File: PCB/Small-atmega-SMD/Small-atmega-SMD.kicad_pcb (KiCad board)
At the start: 2 copper layers, 65.1 x 96.9 mm, 34 parts, among them J1 Daisy port in, J2 ICSP_ISP6, J3 UART, J4 Daisy port out, K1 HYC77-TF09-200, U1 PC817C-S, U2 SE5218, U21 TXB0104QPWRQ1, U3 ATmega328P-AU, Y1 16MHz

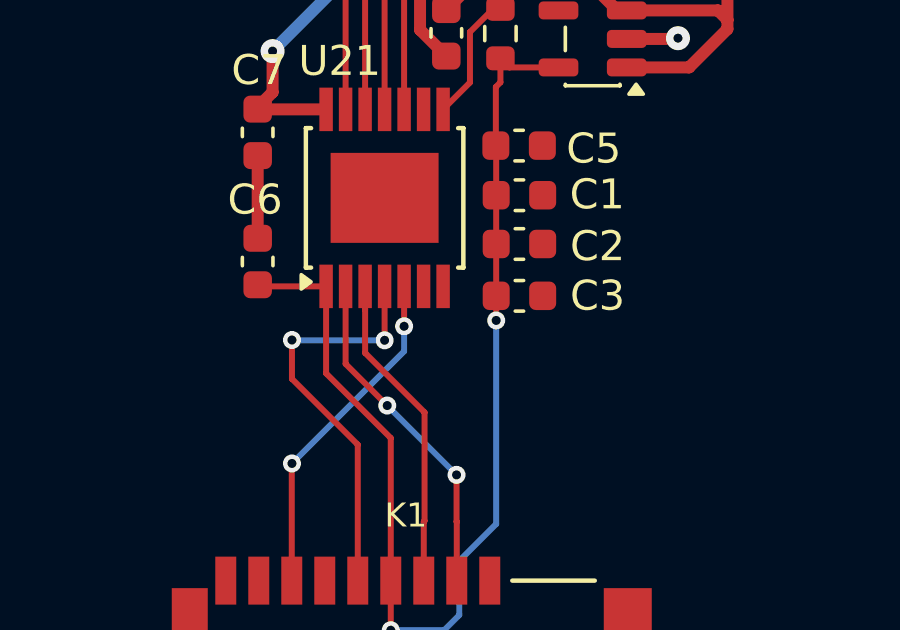
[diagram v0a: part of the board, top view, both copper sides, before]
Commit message: Add GND to level shifter :-/
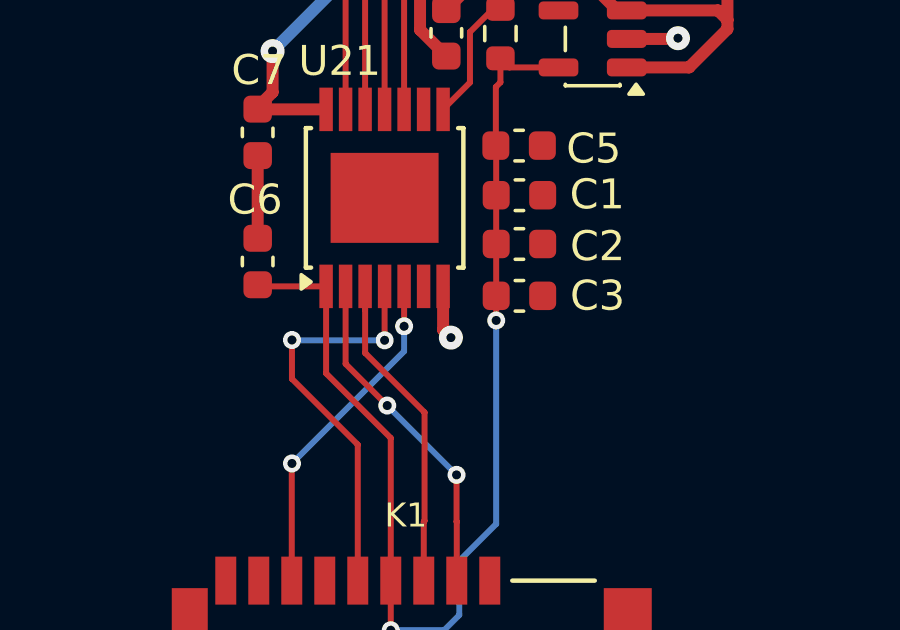
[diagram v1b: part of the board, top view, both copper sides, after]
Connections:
- U21 pad 7: unconnected-(U21-GND-Pad7) -> GND
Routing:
- net GND: track 45.6 -> 47.4 mm, vias 12 -> 13
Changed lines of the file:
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@@
 	(net 47 "OE")
 	(net 48 "unconnected-(U2-NC-Pad4)")
-	(net 49 "unconnected-(U21-GND-Pad7)")
-	(net 50 "unconnected-(U21-NC-Pad9)")
-	(net 51 "unconnected-(U21-NC-Pad6)")
+	(net 49 "unconnected-(U21-NC-Pad9)")
+	(net 50 "unconnected-(U21-NC-Pad6)")
 	(footprint "DSUB-19-angled:DSUB-19_Female_Horizontal_MXS82009-8251-9246"
 		(layer "F.Cu")
@@
 			(net 43 "unconnected-(K1-X-Pad1)")
 			(pinfunction "X")
-			(pintype "bidirectional")
+			(pintype "bidirectional+no_connect")
 		)
 		(pad "2" smd rect
@@
 			(net 46 "unconnected-(K1-X-Pad8)")
 			(pinfunction "X")
-			(pintype "bidirectional")
+			(pintype "bidirectional+no_connect")
 		)
 		(pad "9" smd rect
@@
 			(size 1.45 0.45)
 			(layers "F.Cu" "F.Mask" "F.Paste")
-			(net 51 "unconnected-(U21-NC-Pad6)")
+			(net 50 "unconnected-(U21-NC-Pad6)")
 			(pinfunction "NC")
 			(pintype "no_connect")
@@
 			(size 1.45 0.45)
 			(layers "F.Cu" "F.Mask" "F.Paste")
-			(net 49 "unconnected-(U21-GND-Pad7)")
+			(net 2 "GND")
 			(pinfunction "GND")
 			(pintype "passive")
@@
 			(size 1.45 0.45)
 			(layers "F.Cu" "F.Mask" "F.Paste")
-			(net 50 "unconnected-(U21-NC-Pad9)")
+			(net 49 "unconnected-(U21-NC-Pad9)")
 			(pinfunction "NC")
 			(pintype "no_connect")
@@
 			(net 48 "unconnected-(U2-NC-Pad4)")
 			(pinfunction "NC")
-			(pintype "passive")
+			(pintype "passive+no_connect")
 		)
 		(pad "5" smd roundrect
@@
 	)
 	(segment
+		(start 120.6696 118.2566)
+		(end 120.9294 118.5164)
+		(width 0.4)
+		(layer "F.Cu")
+		(net 2)
+	)
+	(segment
 		(start 129.208 62.0758)
 		(end 128.4224 61.2902)
@@
 	)
 	(segment
+		(start 120.6696 116.8078)
+		(end 120.6696 118.2566)
+		(width 0.4)
+		(layer "F.Cu")
+		(net 2)
+	)
+	(segment
 		(start 123.3932 66.5734)
 		(end 123.3932 64.1096)
@@
 		(size 0.8)
 		(drill 0.3)
+		(layers "F.Cu" "B.Cu")
+		(net 2)
+	)
+	(via
+		(at 120.9294 118.5164)
+		(size 0.8)
+		(drill 0.3)

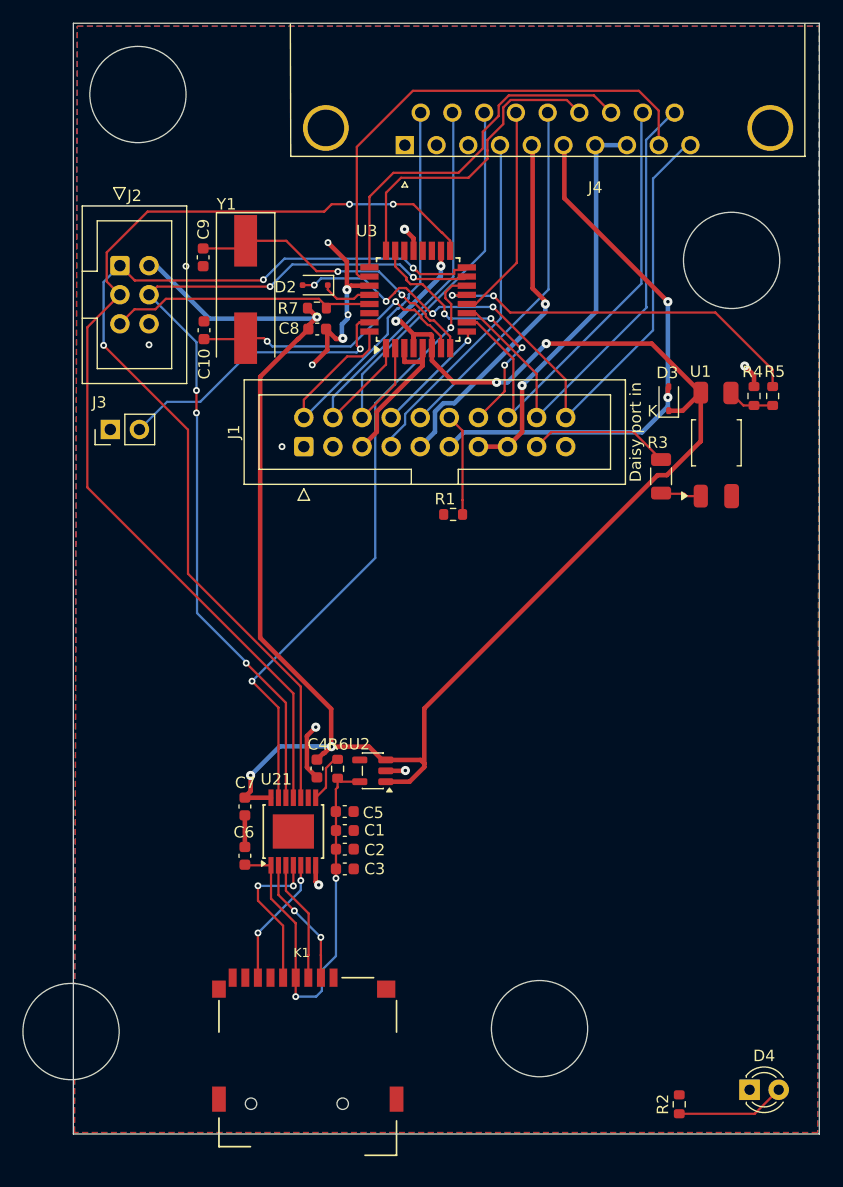
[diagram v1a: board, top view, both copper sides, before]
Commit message: WIP untested very small PCB
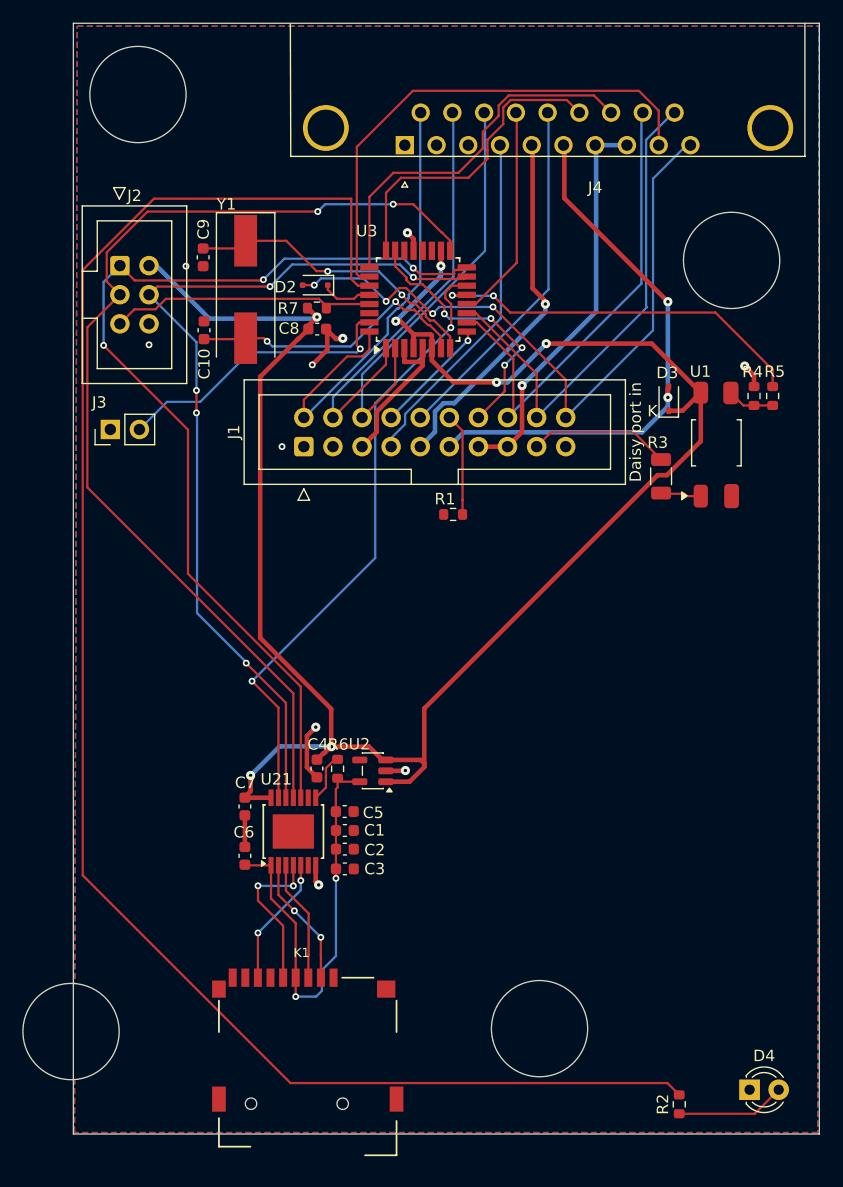
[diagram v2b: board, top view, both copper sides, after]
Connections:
- R2 pad 2: GND -> LED
- U3 pad 27: GND -> LED
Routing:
- net LED: track 0.00 -> 147.7 mm
- net GND: track 47.4 -> 35.5 mm, vias 13 -> 10
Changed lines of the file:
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@@
 	(net 49 "unconnected-(U21-NC-Pad9)")
 	(net 50 "unconnected-(U21-NC-Pad6)")
+	(net 51 "LED")
 	(footprint "DSUB-19-angled:DSUB-19_Female_Horizontal_MXS82009-8251-9246"
 		(layer "F.Cu")
@@
 			(size 1.6 0.55)
 			(layers "F.Cu" "F.Mask" "F.Paste")
-			(net 2 "GND")
+			(net 51 "LED")
 			(pinfunction "PC4")
 			(pintype "tri_state")
@@
 			(layers "F.Cu" "F.Mask" "F.Paste")
 			(roundrect_rratio 0.25)
-			(net 2 "GND")
+			(net 51 "LED")
 			(pintype "passive")
 		)
@@
 			(net 2 "GND")
 			(pinfunction "GND")
-			(pintype "power_in")
+			(pintype "passive")
 		)
 		(pad "3" smd roundrect
@@
 	)
 	(segment
-		(start 129.208 62.0758)
-		(end 128.4224 61.2902)
-		(width 0.4)
-		(layer "F.Cu")
-		(net 2)
-	)
-	(segment
 		(start 130.008 73.200818)
 		(end 126.003 77.205818)
@@
 	)
 	(segment
-		(start 125.358 66.218)
-		(end 123.7486 66.218)
-		(width 0.4)
-		(layer "F.Cu")
-		(net 2)
-	)
-	(segment
-		(start 123.7486 66.218)
-		(end 123.3932 66.5734)
+		(start 121.679 70.104)
+		(end 121.679 71.8182)
 		(width 0.4)
 		(layer "F.Cu")
@@
 	)
 	(segment
-		(start 121.679 70.104)
-		(end 121.679 71.8182)
+		(start 129.208 63.168)
+		(end 129.208 62.1266)
 		(width 0.4)
 		(layer "F.Cu")
@@
 	)
 	(segment
-		(start 123.3932 66.5734)
-		(end 123.3932 64.1096)
-		(width 0.4)
-		(layer "F.Cu")
-		(net 2)
-	)
-	(segment
 		(start 130.008 72.745)
 		(end 130.008 71.668)
@@
 	)
 	(segment
-		(start 123.3932 64.1096)
-		(end 121.7422 62.4586)
+		(start 158.9278 74.041)
+		(end 158.115 73.2282)
 		(width 0.4)
 		(layer "F.Cu")
@@
 	)
 	(segment
-		(start 158.9278 74.041)
-		(end 158.115 73.2282)
+		(start 120.777 109.1314)
+		(end 119.901 108.2554)
 		(width 0.4)
 		(layer "F.Cu")
@@
 	)
 	(segment
-		(start 120.777 109.1314)
-		(end 119.901 108.2554)
+		(start 129.208 62.1266)
+		(end 128.6764 61.595)
 		(width 0.4)
 		(layer "F.Cu")
@@
 		(net 2)
 	)
-	(segment
-		(start 129.208 63.168)
-		(end 129.208 62.0758)
-		(width 0.4)
-		(layer "F.Cu")
-		(net 2)
-	)
 	(via
 		(at 120.3706 73.1266)
@@
 	)
 	(via
-		(at 123.4948 68.7578)
-		(size 0.6)
-		(drill 0.3)
-		(layers "F.Cu" "B.Cu")
-		(free yes)
-		(net 2)
-	)
-	(via
 		(at 123.0376 70.8152)
 		(size 0.8)
@@
 	)
 	(via
-		(at 123.3932 66.5734)
-		(size 0.8)
-		(drill 0.3)
-		(layers "F.Cu" "B.Cu")
-		(net 2)
-	)
-	(via
 		(at 109.347 64.516)
 		(size 0.6)
@@
 	)
 	(via
-		(at 106.1212 71.374)
-		(size 0.6)
+		(at 128.6764 61.595)
+		(size 0.8)
 		(drill 0.3)
 		(layers "F.Cu" "B.Cu")
-		(free yes)
 		(net 2)
 	)
 	(via
-		(at 121.7422 62.4586)
+		(at 106.1212 71.374)
 		(size 0.6)
 		(drill 0.3)
@@
 	)
 	(via
-		(at 128.4224 61.2902)
-		(size 0.8)
-		(drill 0.3)
-		(layers "F.Cu" "B.Cu")
-		(net 2)
-	)
-	(via
 		(at 120.6754 104.7496)
 		(size 0.8)
@@
 	)
 	(segment
-		(start 123.4948 68.7578)
-		(end 123.436763 68.815837)
-		(width 0.4)
-		(layer "B.Cu")
-		(net 2)
-	)
-	(segment
-		(start 122.956001 69.594162)
-		(end 122.956001 70.733601)
-		(width 0.4)
-		(layer "B.Cu")
-		(net 2)
-	)
-	(segment
-		(start 123.3932 68.6562)
-		(end 123.4948 68.7578)
-		(width 0.4)
-		(layer "B.Cu")
-		(net 2)
-	)
-	(segment
-		(start 123.436763 68.815837)
-		(end 123.436763 69.1134)
-		(width 0.4)
-		(layer "B.Cu")
-		(net 2)
-	)
-	(segment
-		(start 122.956001 70.733601)
-		(end 123.0376 70.8152)
-		(width 0.4)
-		(layer "B.Cu")
-		(net 2)
-	)
-	(segment
-		(start 123.436763 69.1134)
-		(end 122.956001 69.594162)
-		(width 0.4)
-		(layer "B.Cu")
-		(net 2)
-	)
-	(segment
-		(start 123.3932 66.5734)
-		(end 123.3932 68.6562)
-		(width 0.4)
-		(layer "B.Cu")
-		(net 2)
-	)
-	(segment
 		(start 123.4186 72.39)
 		(end 119.634 76.1746)
@@
 	)
 	(segment
-		(start 122.0594 59.1058)
-		(end 121.4182 59.747)
-		(width 0.2)
-		(layer "F.Cu")
-		(net 14)
-	)
-	(segment
-		(start 102.4302 63.3142)
-		(end 102.4302 65.8542)
-		(width 0.2)
-		(layer "F.Cu")
-		(net 14)
-	)
-	(segment
 		(start 100.7364 69.85)
 		(end 100.7364 83.82)
@@
 	)
 	(segment
-		(start 123.6218 59.1058)
-		(end 122.0594 59.1058)
+		(start 102.4302 63.3142)
+		(end 102.4302 65.8542)
 		(width 0.2)
 		(layer "F.Cu")
@@
 	)
 	(segment
-		(start 121.4182 59.747)
-		(end 105.9974 59.747)
+		(start 102.4302 65.8542)
+		(end 103.5812 67.0052)
 		(width 0.2)
 		(layer "F.Cu")
@@
 	)
 	(segment
-		(start 102.4302 65.8542)
-		(end 103.5812 67.0052)
+		(start 120.8532 59.747)
+		(end 105.9974 59.747)
 		(width 0.2)
 		(layer "F.Cu")
@@
 	)
 	(via
-		(at 123.6218 59.1058)
+		(at 120.8532 59.747)
 		(size 0.6)
 		(drill 0.3)
@@
 	)
 	(segment
-		(start 123.6218 59.1058)
+		(start 121.4944 59.1058)
 		(end 127.4318 59.1058)
 		(width 0.2)
@@
 	)
 	(segment
+		(start 120.8532 59.747)
+		(end 121.4944 59.1058)
+		(width 0.2)
+		(layer "B.Cu")
+		(net 14)
+	)
+	(segment
 		(start 128.593 65.513057)
 		(end 127.608 64.528057)
@@
 	)
 	(segment
+		(start 118.1018 62.298)
+		(end 114.554 62.298)
+		(width 0.2)
+		(layer "F.Cu")
+		(net 29)
+	)
+	(segment
 		(start 132.408 70.668)
 		(end 132.408 71.668)
@@
 	)
 	(segment
-		(start 122.6058 64.9828)
-		(end 122.5708 64.9478)
+		(start 121.701 64.9478)
+		(end 120.7516 64.9478)
 		(width 0.2)
 		(layer "F.Cu")
@@
 	)
 	(segment
-		(start 130.993815 69.253815)
-		(end 132.408 70.668)
+		(start 121.7168 64.9636)
+		(end 121.701 64.9478)
 		(width 0.2)
 		(layer "F.Cu")
@@
 	)
 	(segment
-		(start 122.5708 64.9478)
-		(end 120.7516 64.9478)
+		(start 130.993815 69.253815)
+		(end 132.408 70.668)
 		(width 0.2)
 		(layer "F.Cu")
@@
 	)
 	(segment
-		(start 118.1018 62.298)
-		(end 114.554 62.298)
-		(width 0.2)
-		(layer "F.Cu")
-		(net 29)
-	)
-	(segment
 		(start 113.886 62.966)
 		(end 114.554 62.298)
@@
 	)
 	(via
-		(at 122.6058 64.9828)
+		(at 121.7168 64.9636)
 		(size 0.6)
 		(drill 0.3)
@@
 	)
 	(segment
-		(start 122.6058 64.9828)
-		(end 122.625 64.9636)
+		(start 128.1938 66.9798)
+		(end 128.1938 67.021)
 		(width 0.2)
 		(layer "B.Cu")
@@
 	)
 	(segment
-		(start 128.1938 66.9798)
-		(end 128.1938 67.021)
-		(width 0.2)
-		(layer "B.Cu")
-		(net 29)
-	)
-	(segment
-		(start 122.625 64.9636)
+		(start 121.7168 64.9636)
 		(end 126.1776 64.9636)
 		(width 0.2)
@@
 		(net 47)
 	)
+	(segment
+		(start 100.3354 64.8419)
+		(end 100.3354 117.6782)
+		(width 0.2)
+		(layer "F.Cu")
+		(net 51)
+	)
+	(segment
+		(start 151.372 135.815)
+		(end 152.4 136.843)
+		(width 0.2)
+		(layer "F.Cu")
+		(net 51)
+	)
+	(segment
+		(start 124.358 66.218)
+		(end 123.7742 65.6342)
+		(width 0.2)
+		(layer "F.Cu")
+		(net 51)
+	)
+	(segment
+		(start 106.5541 58.6232)
+		(end 100.3354 64.8419)
+		(width 0.2)
+		(layer "F.Cu")
+		(net 51)
+	)
+	(segment
+		(start 123.7742 58.6232)
+		(end 106.5541 58.6232)
+		(width 0.2)
+		(layer "F.Cu")
+		(net 51)
+	)
+	(segment
+		(start 118.4722 135.815)
+		(end 151.372 135.815)
+		(width 0.2)
+		(layer "F.Cu")
+		(net 51)
+	)
+	(segment
+		(start 100.3354 117.6782)
+		(end 118.4722 135.815)
+		(width 0.2)
+		(layer "F.Cu")
+		(net 51)
+	)
+	(segment
+		(start 123.7742 65.6342)
+		(end 123.7742 58.6232)
+		(width 0.2)
+		(layer "F.Cu")
+		(net 51)
+	)
+	(segment
+		(start 125.358 66.218)
+		(end 124.358 66.218)
+		(width 0.2)
+		(layer "F.Cu")
+		(net 51)
+	)
 	(zone

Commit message: Move connector away from MCU
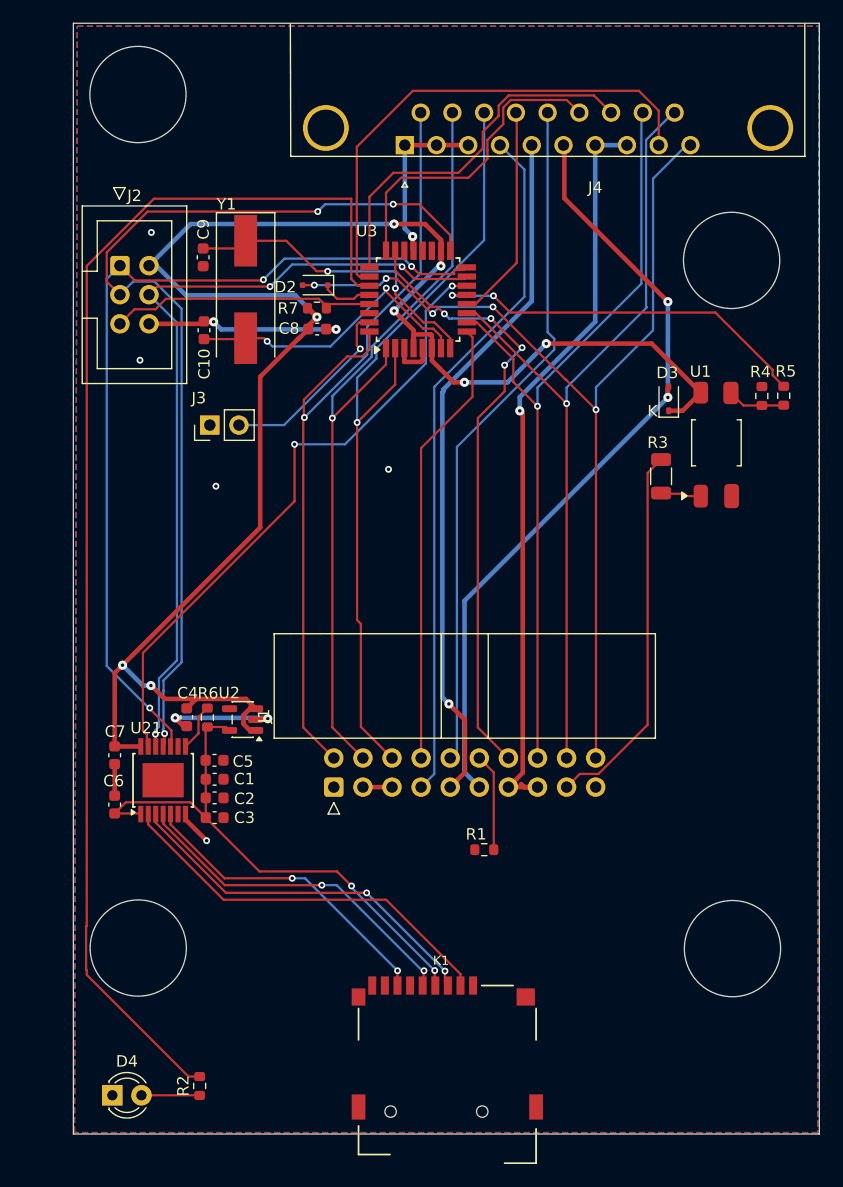
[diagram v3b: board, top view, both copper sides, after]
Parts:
- J1: footprint Connector_IDC:IDC-Header_2x10_P2.54mm_Vertical -> Connector_IDC:IDC-Header_2x10_P2.54mm_Horizontal
- moved D4 55.6 mm to (102.9, 136.9)
- moved R2 41.9 mm to (110.5, 136.1)
- moved J1 29.8 mm to (122.3, 110.0)
- moved R1 29.4 mm to (135.4, 115.4)
- moved REF** 18.2 mm to (157.0, 124.1)
- moved C5 12.2 mm to (111.8, 107.6)
- moved U2 12.2 mm to (114.3, 104.1)
- moved C7 12.2 mm to (103.1, 107.2)
- moved C1 12.2 mm to (111.8, 109.3)
- moved C2 12.2 mm to (111.8, 110.9)
- moved C3 12.2 mm to (111.8, 112.6)
- moved C4 12.2 mm to (109.4, 103.9)
- moved C6 12.2 mm to (103.1, 111.5)
- moved R6 12.2 mm to (111.2, 103.9)
- moved U21 12.2 mm to (107.4, 109.4)
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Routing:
- net LED: track 147.7 -> 109.8 mm
- net PH2: track 38.3 -> 70.1 mm, vias 0 -> 1
- net +12V: track 34.9 -> 66.2 mm
- net PH1: track 39.0 -> 69.8 mm, vias 0 -> 1
- net PH0: track 41.6 -> 72.3 mm, vias 0 -> 1
- net DRV1_in: track 23.6 -> 54.1 mm
- net EN3.5: track 30.3 -> 60.6 mm
- net WREQ: track 31.3 -> 60.3 mm
- net PH3_in: track 10.3 -> 39.3 mm, vias 1 -> 0
- net -12V: track 31.9 -> 60.6 mm
- net WRDATA: track 43.8 -> 72.2 mm, vias 0 -> 1
- net RDDATA_in: track 42.8 -> 71.1 mm, vias 0 -> 1
- net WRPROT_out: track 60.4 -> 88.4 mm, vias 4 -> 5
- net CS_L: track 11.3 -> 34.6 mm, vias 2 -> 0
- net MOSI_L: track 10.6 -> 32.7 mm, vias 0 -> 2
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
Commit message: Switch to resonator
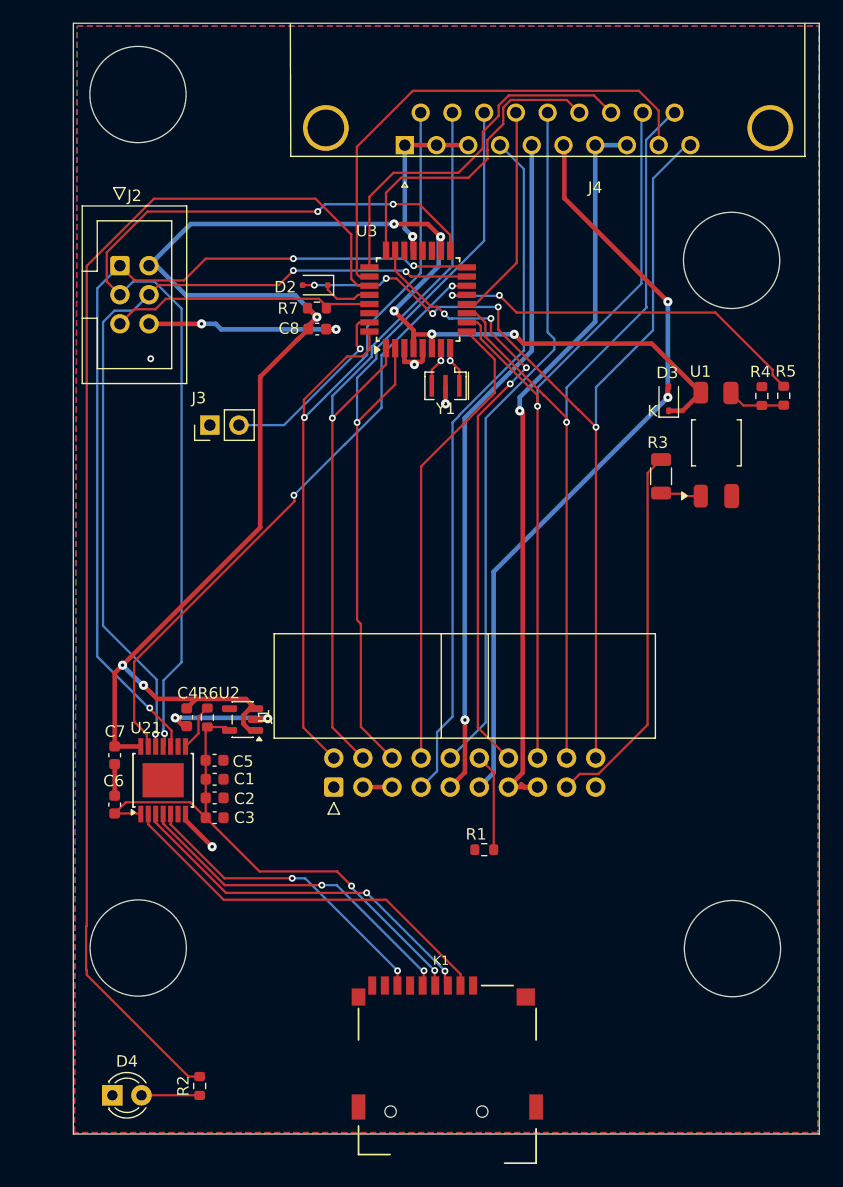
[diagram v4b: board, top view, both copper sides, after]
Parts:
- removed C10, C9: 22pF, Capacitor_SMD:C_0603_1608Metric
- Y1: value 16MHz -> Crystal_GND2; footprint Crystal:Crystal_SMD_HC49-SD -> Crystal:Resonator_SMD_Murata_CSTxExxV-3Pin_3.0x1.1mm
- moved Y1 19.4 mm to (132.0, 75.0), turned to 180 degrees
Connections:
- Y1 pad 2: Net-(U3-XTAL1/PB6) -> GND
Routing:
- net Net-(U3-XTAL2/PB7): track 26.5 -> 3.62 mm, vias 2 -> 1
- net Net-(U3-XTAL1/PB6): track 26.1 -> 3.62 mm, vias 2 -> 1
- net GND: track 55.0 -> 57.7 mm, vias 10 -> 9
- net MOSI: track 70.6 -> 72.8 mm
- net CS: track 55.3 -> 53.4 mm
- net LED: track 109.8 -> 108.0 mm
- net WRPROT_out: track 88.4 -> 90.2 mm
- net WRDATA: track 72.2 -> 73.9 mm
- net -12V: track 60.6 -> 59.0 mm
- net PH3_in: track 39.3 -> 40.9 mm
- net 5V_apple2: track 68.6 -> 67.5 mm
- net 5V_burgerDisk: track 157.2 -> 158.0 mm
